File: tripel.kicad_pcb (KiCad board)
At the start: 2 copper layers, 95.1 x 97.5 mm, 73 parts, among them J1 Left Columns, J2 Left Rows, J3 Right Rows, J4 Right Columns, J5 Left Rows, J6 USB_mini_micro_B, J7 Conn_01x04, J8 Right Rows, K1.1 KEYSW, K1.2 KEYSW, K1.3 KEYSW, K1.4 KEYSW, K1.5 KEYSW, K2.1 KEYSW, K2.2 KEYSW, K2.3 KEYSW, K2.4 KEYSW, K2.5 KEYSW, K3.1 KEYSW, K3.2 KEYSW, K3.3 KEYSW, K3.4 KEYSW, K3.5 KEYSW, K4.1 KEYSW, K4.2 KEYSW, K4.3 KEYSW, K4.4 KEYSW, K4.5 KEYSW, K5.1_1.5u1 KEYSW, K5.1_1u1 KEYSW, K5.1_1u2 KEYSW, K5.2_1.5u1 KEYSW, K5.2_1u1 KEYSW, K5.2_1u2 KEYSW, K5.3_1.5u1 KEYSW, K5.3_1u1 KEYSW, K5.3_7u1 KEYSW, K5.4_1.5u1 KEYSW, K5.4_1u1 KEYSW, U1 ProMicro_ChipSideDown

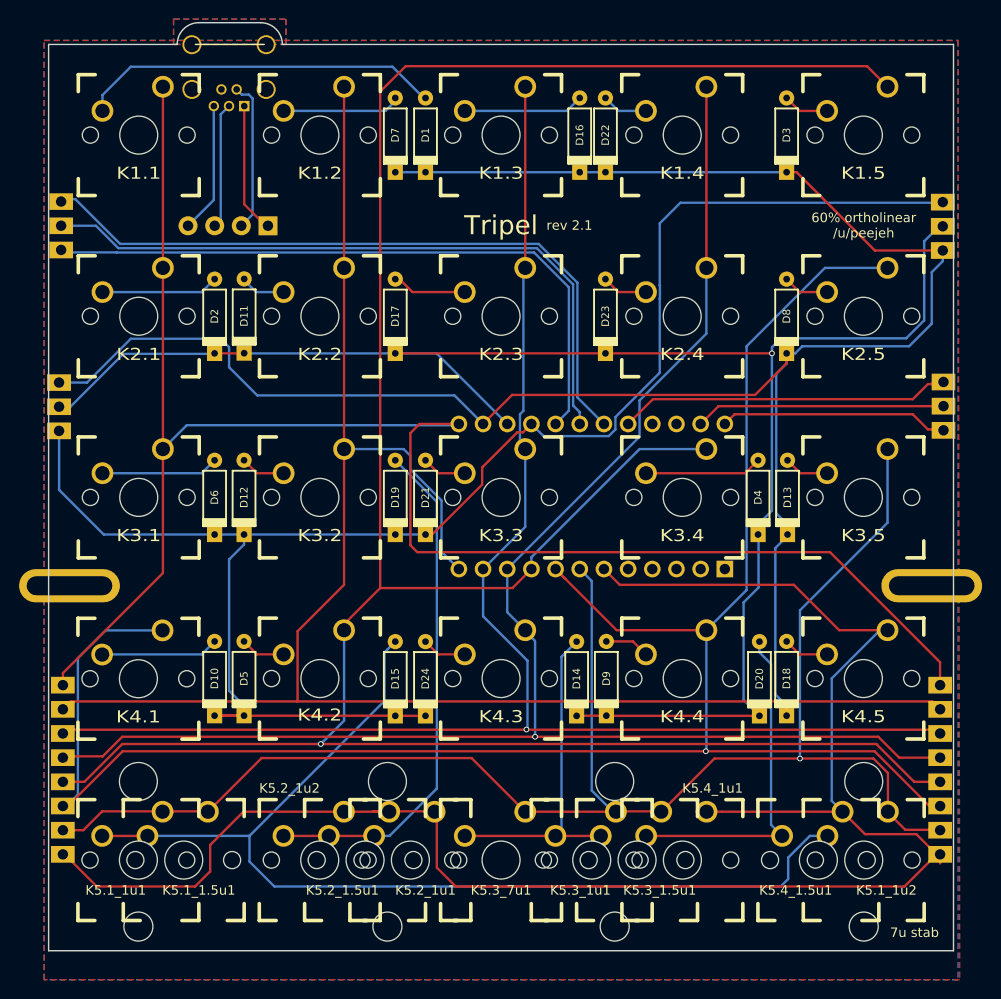
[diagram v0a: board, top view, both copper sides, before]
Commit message: Breakout reset pads
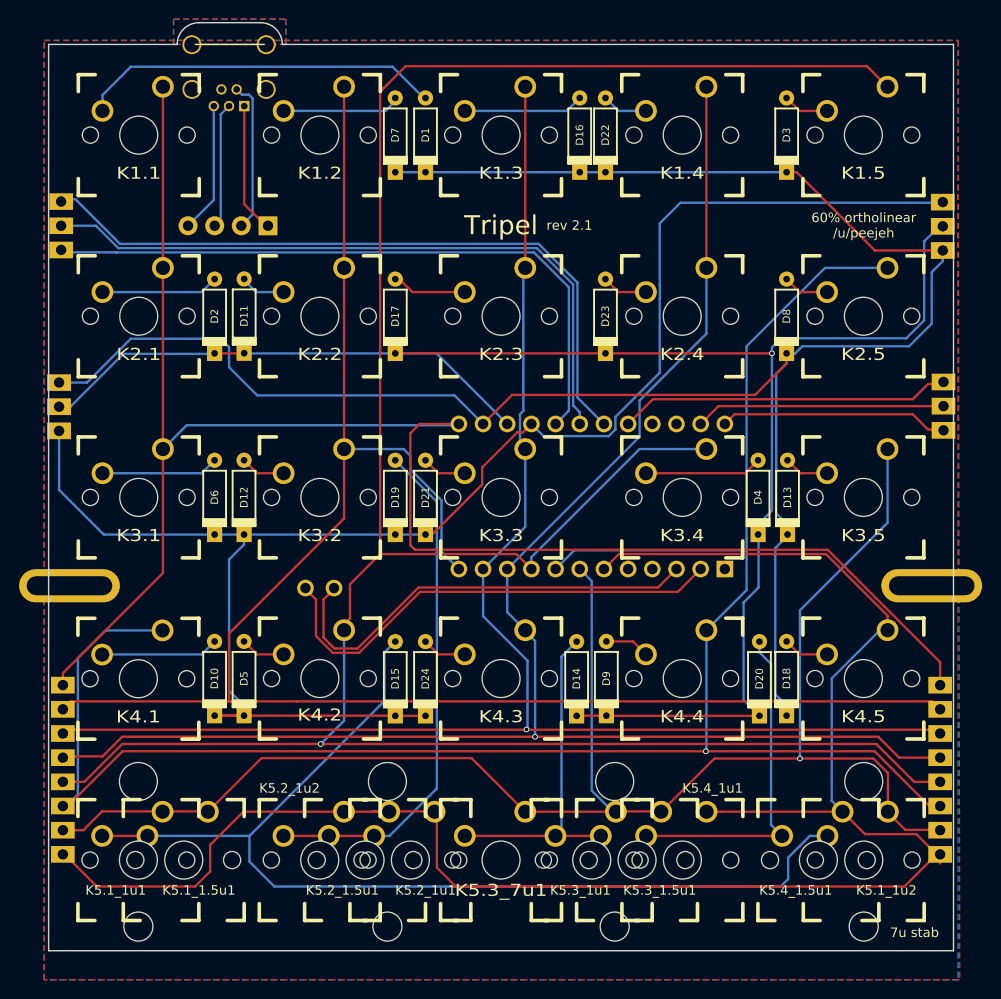
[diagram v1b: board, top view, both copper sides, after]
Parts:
- added J9: Conn_01x02, keyboard:PADS_2, B.Cu at (140.3, 95.2)
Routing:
- net Net-(J9-Pad1): track 0.00 -> 50.3 mm
- net Net-(J9-Pad2): track 0.00 -> 46.7 mm
- net Net-(J1-Pad7): track 181.3 -> 184.3 mm
- net Net-(J1-Pad1): track 191.8 -> 194.0 mm
- net Net-(J1-Pad3): track 206.5 -> 207.4 mm

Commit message: Rename diodes to match the name of their corrisponding switch
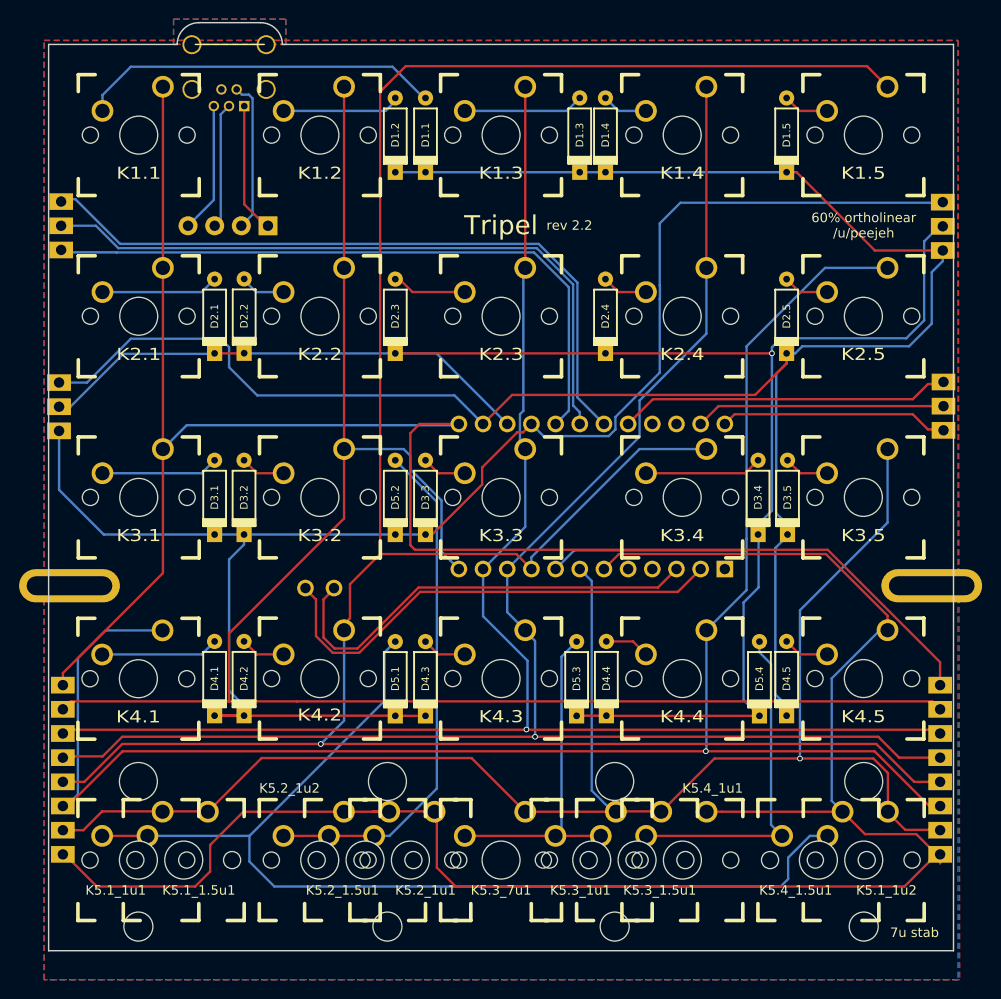
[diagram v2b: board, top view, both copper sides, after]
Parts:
- renumbered D1 to D1.1, D7 to D1.2, D16 to D1.3, D22 to D1.4, D3 to D1.5, D2 to D2.1, D11 to D2.2, D17 to D2.3, D23 to D2.4, D8 to D2.5, D6 to D3.1, D12 to D3.2, D21 to D3.3, D4 to D3.4, D13 to D3.5, D10 to D4.1, D5 to D4.2, D24 to D4.3, D9 to D4.4, D18 to D4.5, D15 to D5.1, D19 to D5.2, D14 to D5.3, D20 to D5.4
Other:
- board text added: "rev 2.2"
- board text removed: "rev 2.1"

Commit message: Move USB pads to more convenient location
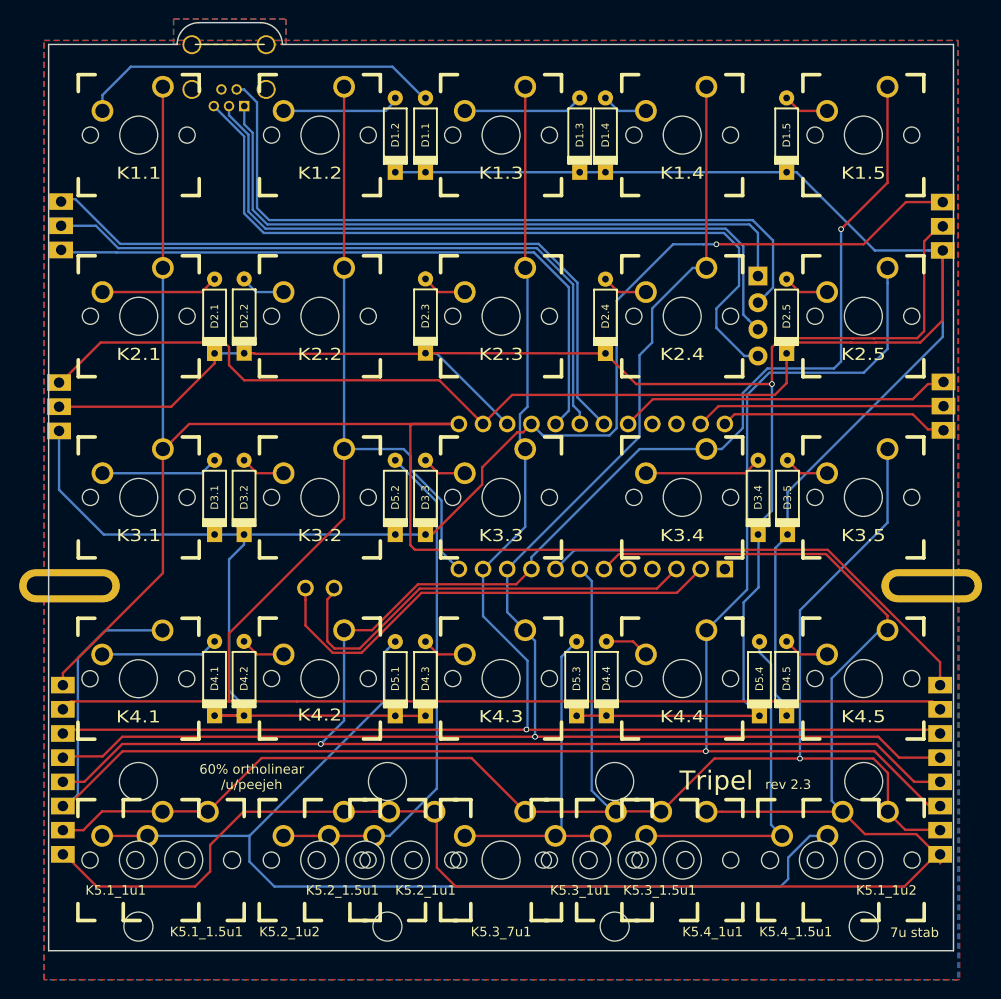
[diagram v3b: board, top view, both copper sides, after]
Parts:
- moved J7 56.5 mm to (186.4, 66.6), turned to 270 degrees
- moved D2.3 3.18 mm to (151.4, 66.6)
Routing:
- net Net-(J6-Pad5): track 13.7 -> 81.1 mm
- net Net-(J6-Pad3): track 13.2 -> 74.8 mm
- net Net-(J6-Pad2): track 15.9 -> 76.6 mm
- net Net-(J1-Pad4): track 263.0 -> 206.4 mm, vias 1 -> 2
- net Net-(J6-Pad1): track 13.7 -> 69.9 mm
- net Net-(D1.1-Pad1): track 212.3 -> 230.2 mm
- net Net-(D2.3-Pad2): track 7.42 -> 4.71 mm
- net Net-(D3.1-Pad1): track 173.0 -> 170.8 mm, vias 0 -> 1
- net Net-(J1-Pad3): track 207.4 -> 209.4 mm
- net Net-(J1-Pad5): track 172.1 -> 173.0 mm
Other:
- board text added: "rev 2.3"
- board text removed: "rev 2.2"

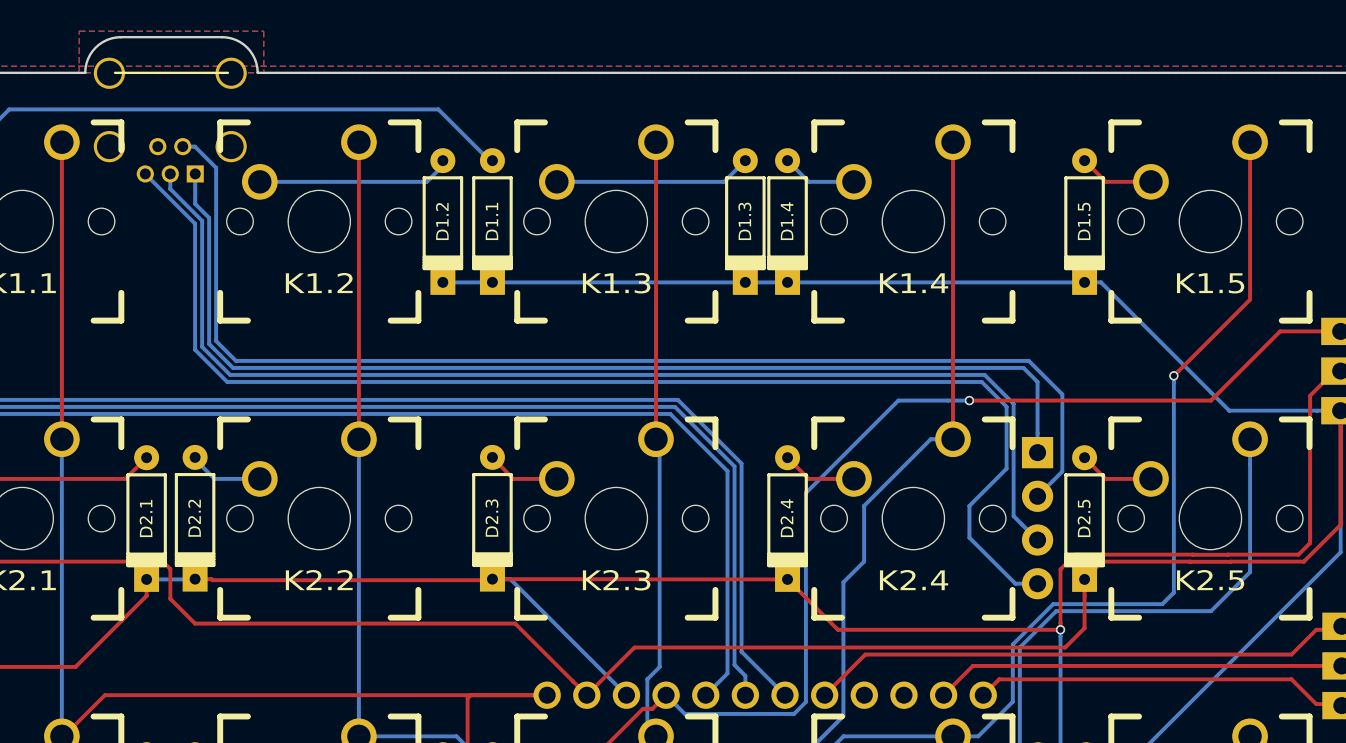
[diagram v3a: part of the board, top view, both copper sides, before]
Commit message: Flip USB footprint to correct side of board
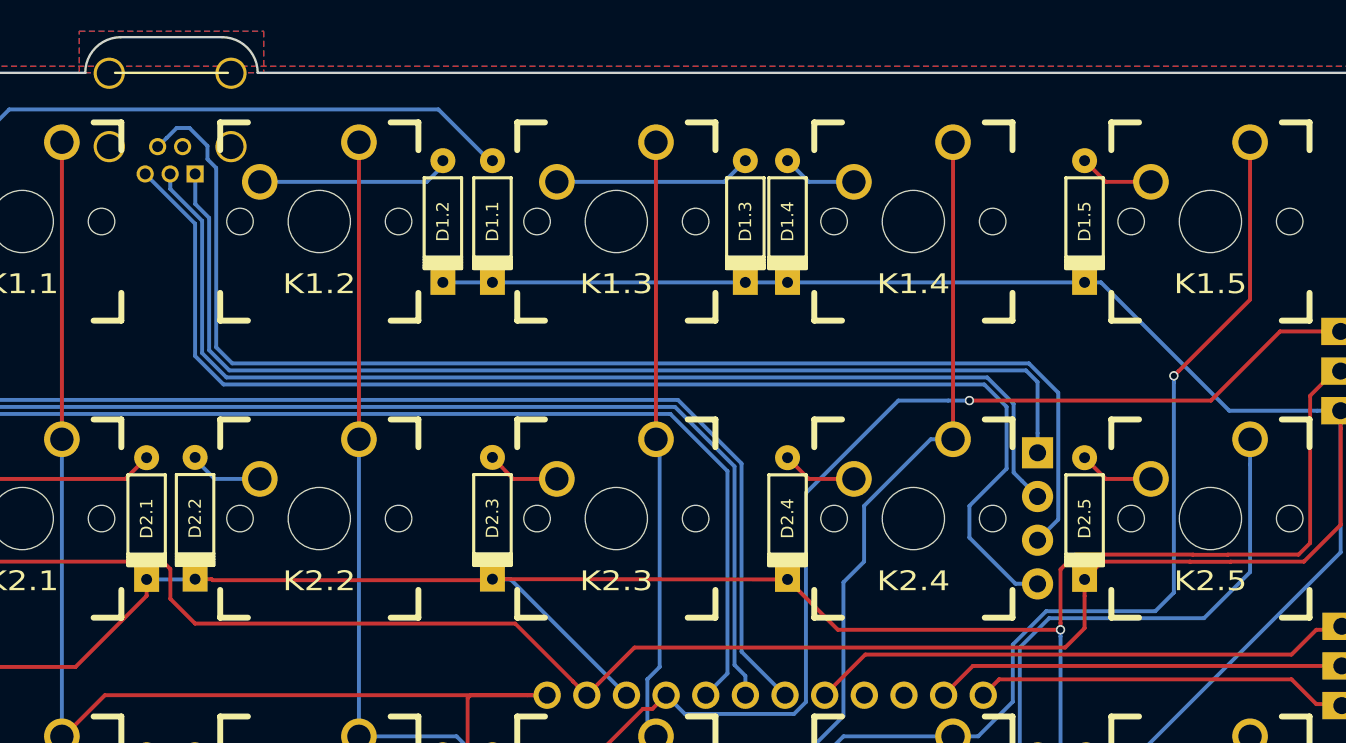
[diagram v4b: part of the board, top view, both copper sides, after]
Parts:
- turned J7 to 90 degrees
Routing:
- net Net-(J6-Pad1): track 69.9 -> 81.3 mm
- net Net-(J6-Pad5): track 81.1 -> 70.1 mm
- net Net-(J6-Pad2): track 76.6 -> 82.4 mm
- net Net-(J6-Pad3): track 74.8 -> 72.2 mm
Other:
- board text added: "USB"

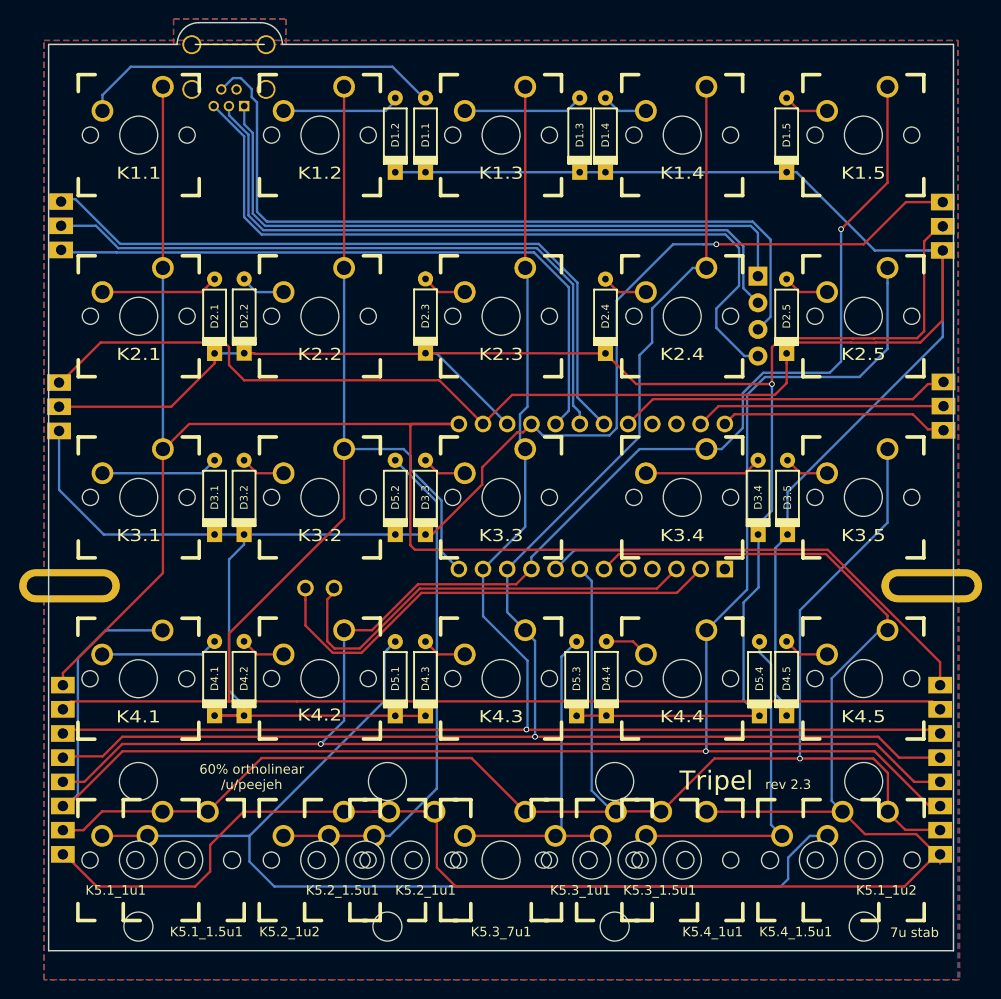
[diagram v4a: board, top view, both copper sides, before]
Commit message: Add switch footprints for alternative mod sizes
This introduces a number of changes so as toallow standard sized mod keys to be used. This required moving of a number of components so as to make space for 2u key stabilizers.

Changes include:
 * Move Pro-Micro to the right to avoid stabilizer mounting holes
 * Add extra connections between boards to allow Pro-Micro to be placed on any of the PCBs
 * Remove USB pertrusion and flip orientation of K1.2 to be north facing
 * Add extra connections so that reset pads can be accessed via hole in case even in Pro-Micro is on a different PCB
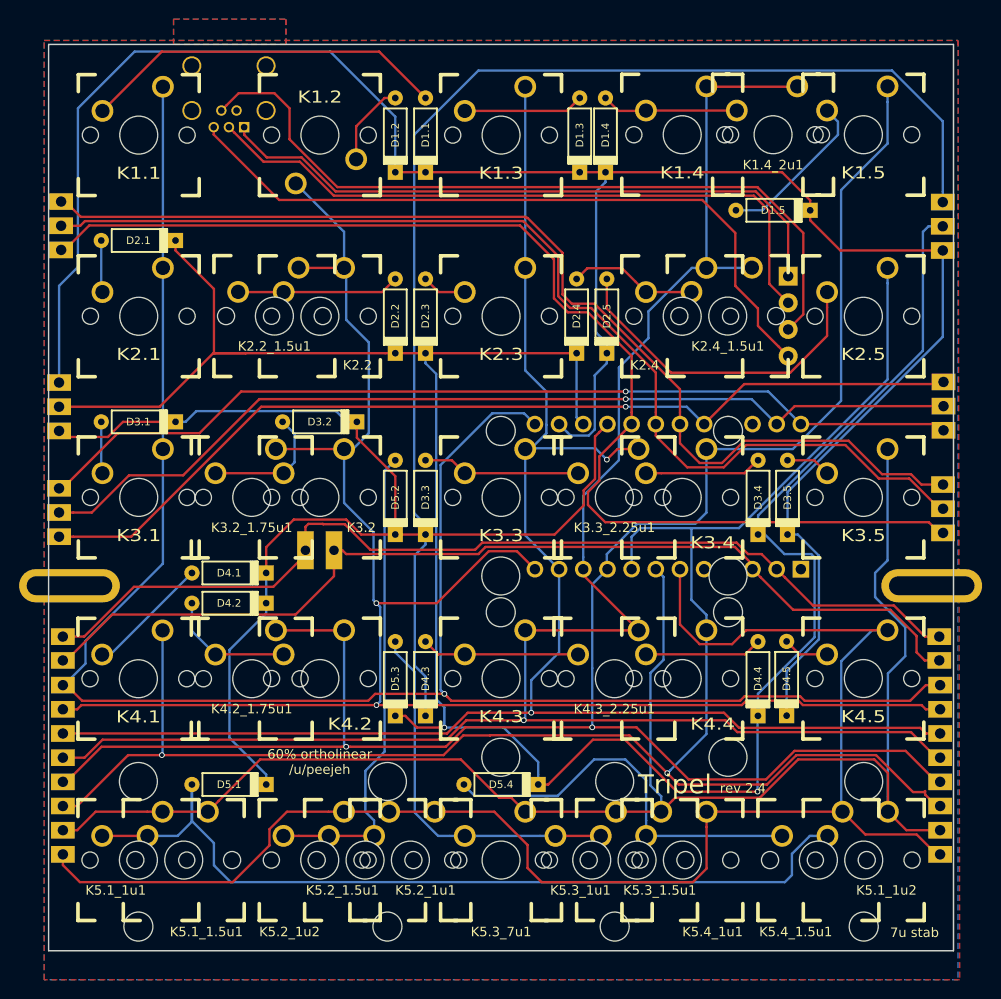
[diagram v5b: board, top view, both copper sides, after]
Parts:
- added J10: Right Reset, keyboard:CONNECTOR_2, B.Cu at (113.3, 101.6)
- added J11: Left Reset, keyboard:CONNECTOR_2, B.Cu at (205.4, 101.6)
- added J12: Far Left Rows, keyboard:CONNECTOR_3, B.Cu at (205.8, 86.9)
- added J13: Far Left Rows, keyboard:CONNECTOR_3, B.Cu at (112.9, 87.3)
- added K1.4_2u1: KEYSW, keyboard:MX, F.Cu at (187.9, 47.6)
- added K2.2_1.5u1: KEYSW, keyboard:MX_PCB_150H, F.Cu at (135.6, 66.6)
- added K2.4_1.5u1: KEYSW, keyboard:MX_PCB_150H, F.Cu at (183.2, 66.6)
- added K3.2_1.75u1: KEYSW, keyboard:MX_PCB_175H, F.Cu at (133.2, 85.7)
- added K3.3_2.25u1: KEYSW, keyboard:MX_PCB_225H, F.Cu at (171.3, 85.7)
- added K4.2_1.75u1: KEYSW, keyboard:MX_PCB_175H, F.Cu at (133.2, 104.7)
- added K4.3_2.25u1: KEYSW, keyboard:MX_PCB_225H, F.Cu at (171.3, 104.7)
- J9: value Conn_01x02 -> Reset; footprint keyboard:PADS_2 -> keyboard:RESET
- moved D5.4 29.3 mm to (159.4, 115.8), turned to 180 degrees
- moved D5.1 20.7 mm to (130.8, 115.8), turned to 180 degrees
- moved D5.3 19.1 mm to (148.3, 104.7)
- moved D2.5 18.9 mm to (170.5, 66.6)
- moved D4.4 15.9 mm to (186.4, 104.7)
- moved D2.2 15.9 mm to (148.3, 66.6)
- moved D2.1 11.3 mm to (121.3, 58.7), turned to 180 degrees
- moved D3.1 11.3 mm to (121.3, 77.8), turned to 180 degrees
- moved D3.2 11.2 mm to (140.3, 77.8), turned to 180 degrees
- moved D4.1 11.2 mm to (130.8, 93.6), turned to 180 degrees
- moved D4.2 8.07 mm to (130.8, 96.8), turned to 180 degrees
- moved D1.5 8.03 mm to (187.9, 55.5), turned to 180 degrees
- moved U1 7.99 mm to (178.4, 85.6)
- moved J9 3.97 mm to (140.3, 91.2)
- moved J7 3.17 mm to (189.5, 66.6)
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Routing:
- net Net-(D3.1-Pad1): track 170.8 -> 252.3 mm, vias 1 -> 0
- net Net-(J13-Pad3): track 24.1 -> 98.8 mm, vias 0 -> 1
- net Net-(J13-Pad2): track 26.3 -> 99.7 mm, vias 0 -> 1
- net Net-(J13-Pad1): track 35.0 -> 101.2 mm, vias 0 -> 1
- net Net-(D2.1-Pad1): track 180.1 -> 243.4 mm, vias 1 -> 2
- net Net-(J10-Pad2): track 46.3 -> 105.4 mm
- net Net-(J12-Pad1): track 69.8 -> 125.2 mm
- net Net-(J10-Pad1): track 50.3 -> 104.2 mm
- net Net-(J12-Pad2): track 71.3 -> 113.7 mm
- net Net-(J12-Pad3): track 73.9 -> 112.8 mm
- net Net-(J1-Pad1): track 194.0 -> 162.2 mm
- net Net-(D2.5-Pad2): track 4.82 -> 35.2 mm
- net Net-(J1-Pad5): track 173.0 -> 197.0 mm
- net Net-(D5.1-Pad2): track 110.3 -> 91.9 mm
- net Net-(J1-Pad8): track 180.3 -> 198.6 mm, vias 0 -> 1
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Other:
- board size 95.1 x 97.5 mm -> 95.1 x 95.2 mm
- board text added: "Chip side down"
- board text added: "rev 2.4"
- board text removed: "Middle PCB only"
- board text removed: "To left PCB"
- board text removed: "To right PCB"
- board text removed: "rev 2.3"
